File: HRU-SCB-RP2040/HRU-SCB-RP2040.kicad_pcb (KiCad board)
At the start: 2 copper layers, 42 x 55 mm, 60 parts, among them J1 Conn_01x03_Pin, J10 Conn_01x03_Pin, J11 Conn_01x03_Pin, J12 Conn_01x03_Pin, J13 Conn_01x03_Pin, J14 Conn_01x03_Pin, J15 Conn_01x03_Pin, J16 Conn_01x03_Pin, J17 Conn_01x03_Pin, J18 Conn_01x03_Pin, J19 Conn_01x03_Pin, J2 Conn_01x03_Pin, J20 Conn_01x03_Pin, J21 Conn_01x03_Pin, J22 Conn_01x03_Pin, J23 Conn_01x03_Pin, J24 Conn_01x03_Pin, J25 Conn_01x04_Pin, J26 Conn_01x04_Pin, J27 Conn_01x04_MountingPin, J28 Conn_01x04_MountingPin, J29 Conn_02x03_Top_Bottom, J3 Conn_01x03_Pin, J30 Micro_SD_Card_Det_Hirose_DM3AT, J31 Conn_01x02_Pin, J4 Conn_01x03_Pin, J5 Conn_01x03_Pin, J6 Conn_01x03_Pin, J7 Conn_01x03_Pin, J8 Conn_01x03_Pin, J9 Conn_01x03_Pin, Q1 BSS138, Q2 BSS138, Q3 BSS138, Q4 BSS138, U1 RaspberryPi_Pico_W, U2 PCA9685PW, U3 PCA9685PW, U4 NJM7805SDL1, U5 SN65HVD11HD, U6 SN65HVD11HD

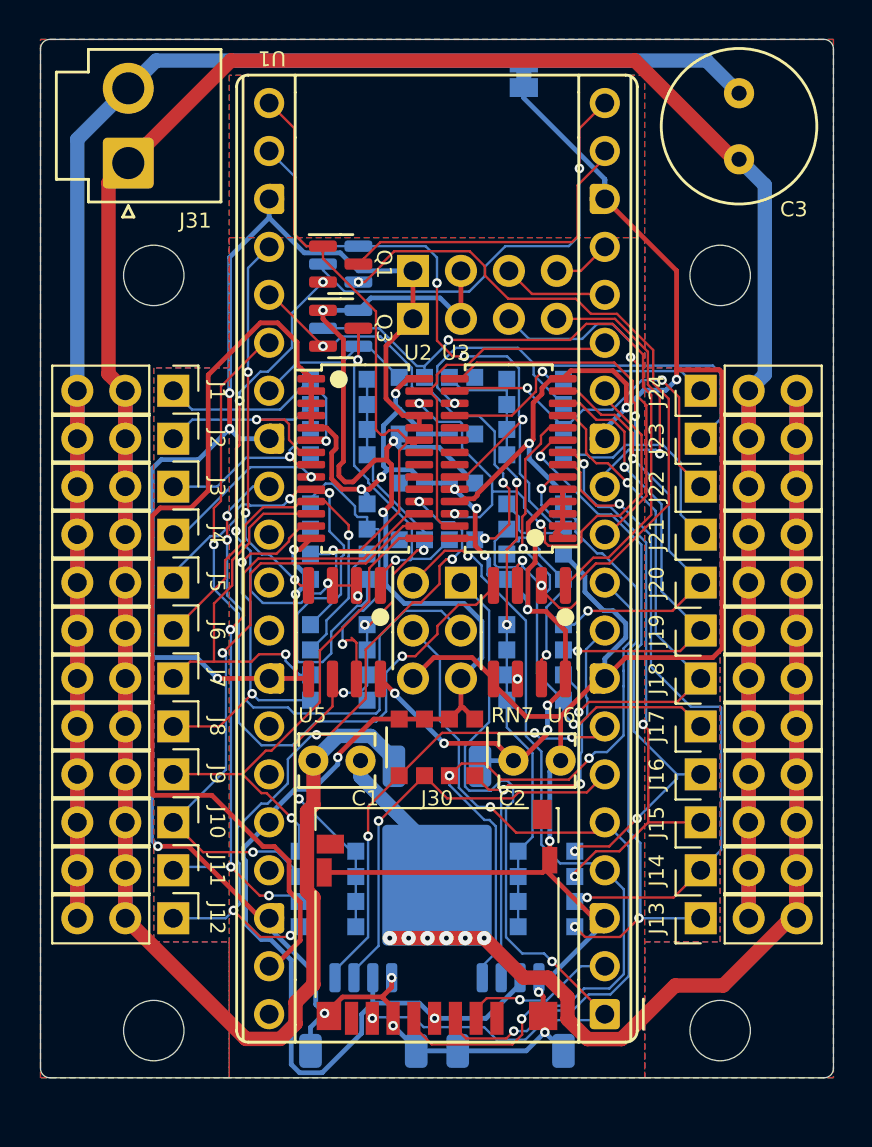
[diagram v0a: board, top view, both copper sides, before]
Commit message: Delete PWM circuit
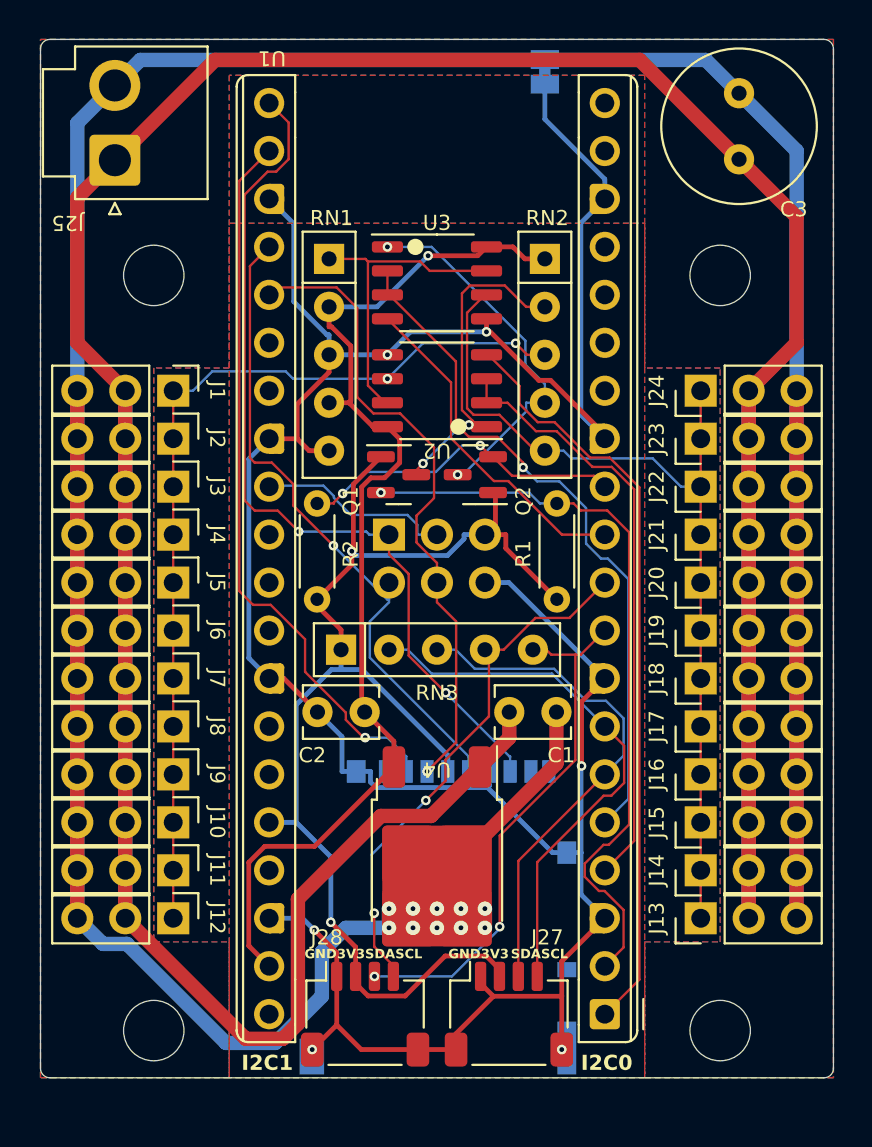
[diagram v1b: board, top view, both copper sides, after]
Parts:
- removed J30: Micro_SD_Card_Det_Hirose_DM3AT, Connector_Card:microSD_HC_Hirose_DM3D-SF
- removed J31: Conn_01x02_Pin, Connector_JST:JST_VH_B2P-VH_1x02_P3.96mm_Vertical
- removed Q3, Q4: BSS138, Package_TO_SOT_SMD:SOT-23
- removed RN10, RN11, RN7, RN8, RN9: 2.2k, Resistor_SMD:R_Array_Convex_4x1206
- removed RN4, RN5, RN6: 100, Resistor_SMD:R_Array_Convex_4x1206
- removed U5, U6: SN65HVD11HD, Package_SO:SOIC-8_3.9x4.9mm_P1.27mm
- added R1: 2.2k, Resistor_THT:R_Axial_DIN0204_L3.6mm_D1.6mm_P5.08mm_Horizontal, F.Cu at (156.3, 124.7)
- added R2: 2.2k, Resistor_THT:R_Axial_DIN0204_L3.6mm_D1.6mm_P5.08mm_Horizontal, F.Cu at (143.7, 124.7)
- J25: value Conn_01x04_Pin -> Conn_01x02_Pin; footprint Connector_PinHeader_2.54mm:PinHeader_1x04_P2.54mm_Vertical -> Connector_JST:JST_VH_B2P-VH_1x02_P3.96mm_Vertical; moved to F.Cu
- J26: value Conn_01x04_Pin -> Micro_SD_Card_Det_Hirose_DM3AT; footprint Connector_PinHeader_2.54mm:PinHeader_1x04_P2.54mm_Vertical -> Connector_Card:microSD_HC_Hirose_DM3AT-SF-PEJM5
- J27, J28, Q2, U4: moved to F.Cu
- RN1, RN2, RN3: value 100 -> 2.2k; footprint Resistor_SMD:R_Array_Convex_4x1206 -> Resistor_THT:R_Array_SIP5; moved to F.Cu
- U2, U3: value PCA9685PW -> MAX485E; footprint Package_SO:TSSOP-28_4.4x9.7mm_P0.65mm -> Package_SO:SOP-8_3.9x4.9mm_P1.27mm
- moved J26 31.7 mm to (150.1, 141.5), turned to 180 degrees
- moved RN2 24.0 mm to (155.7, 106.6), turned to -90 degrees
- moved J25 16.8 mm to (132.9, 101.4), turned to 90 degrees
- moved Q2 13.2 mm to (152.0, 118.1)
- moved RN3 12.7 mm to (144.9, 127.3)
- moved Q1 11.6 mm to (148.0, 118.1)
- moved C1 10.7 mm to (153.8, 130.6)
- moved U3 10.1 mm to (150.0, 107.9), turned to 0 degrees
- moved RN1 8.39 mm to (144.3, 106.6), turned to -90 degrees
- moved C2 8.29 mm to (146.2, 130.6), turned to 180 degrees
- moved J27 7.71 mm to (153.8, 146.6), turned to 0 degrees
- moved J28 7.71 mm to (146.2, 146.6), turned to 0 degrees
- moved U2 5.23 mm to (150.0, 113.6), turned to 180 degrees
- moved J29 4.58 mm to (147.5, 121.2), turned to -90 degrees
- moved JP1 1.13 mm to (155.7, 96.7)
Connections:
- J1 pad 1: /ServoPort/SIG.1 -> /ServoPort/SERVO.SERIAL0
- J10 pad 1: /ServoPort/SIG.10 -> /ServoPort/SERVO.SERIAL0
- J11 pad 1: /ServoPort/SIG.11 -> /ServoPort/SERVO.SERIAL0
- J12 pad 1: /ServoPort/SIG.12 -> /ServoPort/SERVO.SERIAL0
- J13 pad 1: /ServoPort/SIG.13 -> /ServoPort/SERVO.SERIAL1
- J14 pad 1: /ServoPort/SIG.14 -> /ServoPort/SERVO.SERIAL1
- J15 pad 1: /ServoPort/SIG.15 -> /ServoPort/SERVO.SERIAL1
- J16 pad 1: /ServoPort/SIG.16 -> /ServoPort/SERVO.SERIAL1
- J17 pad 1: /ServoPort/SIG.17 -> /ServoPort/SERVO.SERIAL1
- J18 pad 1: /ServoPort/SIG.18 -> /ServoPort/SERVO.SERIAL1
- J19 pad 1: /ServoPort/SIG.19 -> /ServoPort/SERVO.SERIAL1
- J2 pad 1: /ServoPort/SIG.2 -> /ServoPort/SERVO.SERIAL0
- J20 pad 1: /ServoPort/SIG.20 -> /ServoPort/SERVO.SERIAL1
- J21 pad 1: /ServoPort/SIG.21 -> /ServoPort/SERVO.SERIAL1
- J22 pad 1: /ServoPort/SIG.22 -> /ServoPort/SERVO.SERIAL1
- J23 pad 1: /ServoPort/SIG.23 -> /ServoPort/SERVO.SERIAL1
- J24 pad 1: /ServoPort/SIG.24 -> /ServoPort/SERVO.SERIAL1
- J25 pad 1: GND -> VCC
- J25 pad 2: +3V3 -> GNDPWR
- J26 pad 1: GND -> unconnected-(J26-DAT2-Pad1)
- J26 pad 2: +3V3 -> /SPI.CS.SD
- J26 pad 3: /UART1.TX -> /SPI.MOSI
- J26 pad 4: /UART1.RX -> +3V3
- J3 pad 1: /ServoPort/SIG.3 -> /ServoPort/SERVO.SERIAL0
- J4 pad 1: /ServoPort/SIG.4 -> /ServoPort/SERVO.SERIAL0
- J5 pad 1: /ServoPort/SIG.5 -> /ServoPort/SERVO.SERIAL0
- J6 pad 1: /ServoPort/SIG.6 -> /ServoPort/SERVO.SERIAL0
- J7 pad 1: /ServoPort/SIG.7 -> /ServoPort/SERVO.SERIAL0
- J8 pad 1: /ServoPort/SIG.8 -> /ServoPort/SERVO.SERIAL0
- J9 pad 1: /ServoPort/SIG.9 -> /ServoPort/SERVO.SERIAL0
- Q1 pad 1: /SERVO.SERIAL0.EN -> +3V3
- Q1 pad 2: Net-(Q1-S) -> /SERVO.SERIAL0.RX
- Q1 pad 3: /SERVO.SERIAL0.DE -> Net-(Q1-D)
- Q2 pad 1: /SERVO.SERIAL1.EN -> +3V3
- Q2 pad 2: Net-(Q2-S) -> /SERVO.SERIAL1.RX
- Q2 pad 3: /SERVO.SERIAL1.DE -> Net-(Q2-D)
- RN1 pad 1: /ServoPort/SIG.4 -> /ServoPort/SERVO.NULL
- RN1 pad 2: /ServoPort/SIG.3 -> +5V
- RN1 pad 3: /ServoPort/SIG.2 -> GND
- RN1 pad 4: /ServoPort/SIG.1 -> +5V
- RN1 pad 5: /ServoPort/SERVO.SERIAL0 -> GND
- RN2 pad 1: /ServoPort/SIG.8 -> +5V
- RN2 pad 2: /ServoPort/SIG.7 -> Net-(Q1-D)
- RN2 pad 3: /ServoPort/SIG.6 -> /ServoPort/SERVO.SERIAL0
- RN2 pad 4: /ServoPort/SIG.5 -> Net-(Q2-D)
- RN2 pad 5: /ServoPort/SERVO.SERIAL0 -> /ServoPort/SERVO.SERIAL1
- RN3 pad 1: /ServoPort/SIG.12 -> +3V3
- RN3 pad 2: /ServoPort/SIG.11 -> /I2C0.SCL
- RN3 pad 3: /ServoPort/SIG.10 -> /I2C0.SDA
- RN3 pad 4: /ServoPort/SIG.9 -> /I2C1.SCL
- RN3 pad 5: /ServoPort/SERVO.SERIAL0 -> /I2C1.SDA
- U1 pad 1: /SPI.MISO -> /SERVO.SERIAL0.TX
- U1 pad 11: /UART1.TX -> /SERVO.SERIAL1.TX
- U1 pad 12: /UART1.RX -> /SERVO.SERIAL1.RX
- U1 pad 14: /PIO.0 -> unconnected-(U1-GPIO10-Pad14)
- U1 pad 15: /PIO.1 -> unconnected-(U1-GPIO11-Pad15)
- U1 pad 16: /UART0.TX -> unconnected-(U1-GPIO12-Pad16)
- U1 pad 17: /UART0.RX -> unconnected-(U1-GPIO13-Pad17)
- U1 pad 19: /SERVO.SERIAL0.DE -> unconnected-(U1-GPIO14-Pad19)
- U1 pad 2: /SPI.CS.SD -> /SERVO.SERIAL0.RX
- U1 pad 20: /SERVO.SERIAL1.DE -> unconnected-(U1-GPIO15-Pad20)
- U1 pad 21: /SERVO.SERIAL0.EN -> /SPI.MISO
- U1 pad 22: /SERVO.SERIAL1.EN -> /SPI.CS.SD
- U1 pad 24: /PIO.2 -> /SPI.CLK
- U1 pad 25: /PIO.3 -> /SPI.MOSI
- U1 pad 26: /PIO.4 -> unconnected-(U1-GPIO20-Pad26)
- U1 pad 27: /PIO.5 -> unconnected-(U1-GPIO21-Pad27)
- U1 pad 4: /SPI.CLK -> /SERVO.SERIAL0.DE
- U1 pad 5: /SPI.MOSI -> /SERVO.SERIAL1.DE
- U2 pad 1: +5V -> Net-(Q1-D)
- U2 pad 2: +5V -> /SERVO.SERIAL0.DE
- U2 pad 3: +5V -> /SERVO.SERIAL0.DE
- U2 pad 4: +5V -> /SERVO.SERIAL0.TX
- U2 pad 5: +5V -> GND
- U2 pad 6: /ServoPort/SIG.1 -> /ServoPort/SERVO.SERIAL0
- U2 pad 7: /ServoPort/SIG.2 -> /ServoPort/SERVO.NULL
- U2 pad 8: /ServoPort/SIG.3 -> +5V
- U3 pad 1: +5V -> Net-(Q2-D)
- U3 pad 2: +5V -> /SERVO.SERIAL1.DE
- U3 pad 3: +5V -> /SERVO.SERIAL1.DE
- U3 pad 4: +5V -> /SERVO.SERIAL1.TX
- U3 pad 5: +5V -> GND
- U3 pad 6: /ServoPort/SIG.13 -> /ServoPort/SERVO.SERIAL1
- U3 pad 7: /ServoPort/SIG.14 -> /ServoPort/SERVO.NULL
- U3 pad 8: /ServoPort/SIG.15 -> +5V
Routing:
- net GND: track 233.0 -> 150.1 mm, vias 15 -> 6
- net +5V: track 118.0 -> 58.3 mm, vias 11 -> 1
- net /SERVO.SERIAL0.EN: track 48.3 -> 0.00 mm, vias 1 -> 0
- net Net-(Q2-S): track 45.1 -> 0.00 mm, vias 3 -> 0
- net /SERVO.SERIAL1.EN: track 41.4 -> 0.00 mm, vias 3 -> 0
- net /PIO.4: track 41.0 -> 0.00 mm, vias 2 -> 0
- net /SERVO.SERIAL0.TX: track 0.00 -> 40.2 mm
- net /SERVO.SERIAL0.RX: track 0.00 -> 39.6 mm, vias 0 -> 1
- net /ServoPort/SIG.12: track 37.0 -> 0.00 mm, vias 5 -> 0
- net /ServoPort/SIG.14: track 34.8 -> 0.00 mm, vias 2 -> 0
- net Net-(Q4-D): track 34.8 -> 0.00 mm, vias 1 -> 0
- net /ServoPort/SIG.13: track 34.7 -> 0.00 mm, vias 3 -> 0
- net /ServoPort/SIG.11: track 34.0 -> 0.00 mm, vias 3 -> 0
- net /ServoPort/SIG.10: track 33.0 -> 0.00 mm, vias 2 -> 0
- net GNDPWR: track 203.3 -> 235.0 mm, vias 6 -> 10
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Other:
- board text removed: "RX"
- board text removed: "TX"
- board text removed: "UART0"
- board text removed: "UART1"

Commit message: Update design for hand soldering friendly
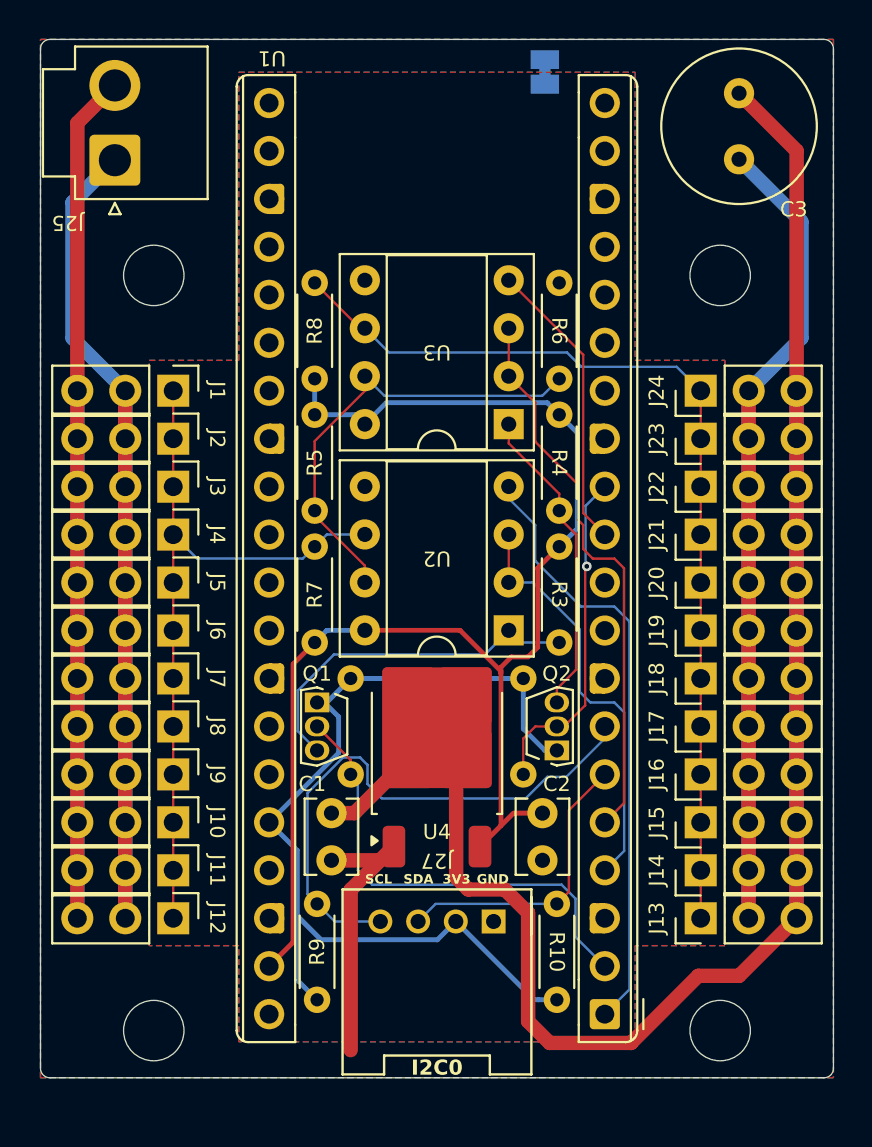
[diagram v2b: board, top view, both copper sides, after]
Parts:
- removed J26: Micro_SD_Card_Det_Hirose_DM3AT, Connector_Card:microSD_HC_Hirose_DM3AT-SF-PEJM5
- removed J28: Conn_01x04_MountingPin, Connector_JST:JST_SH_SM04B-SRSS-TB_1x04-1MP_P1.00mm_Horizontal
- removed J29: Conn_02x03_Top_Bottom, Connector_PinHeader_2.54mm:PinHeader_2x03_P2.54mm_Vertical
- removed RN1, RN2, RN3: 2.2k, Resistor_THT:R_Array_SIP5
- added R10: 2.2k, Resistor_THT:R_Axial_DIN0204_L3.6mm_D1.6mm_P5.08mm_Horizontal, F.Cu at (156.3, 140.8)
- added R3: 2.2k, Resistor_THT:R_Axial_DIN0204_L3.6mm_D1.6mm_P5.08mm_Horizontal, F.Cu at (156.5, 121.9)
- added R4: 2.2k, Resistor_THT:R_Axial_DIN0204_L3.6mm_D1.6mm_P5.08mm_Horizontal, F.Cu at (156.5, 114.9)
- added R5: 2.2k, Resistor_THT:R_Axial_DIN0204_L3.6mm_D1.6mm_P5.08mm_Horizontal, F.Cu at (143.5, 114.9)
- added R6: 2.2k, Resistor_THT:R_Axial_DIN0204_L3.6mm_D1.6mm_P5.08mm_Horizontal, F.Cu at (156.5, 113.0)
- added R7: 2.2k, Resistor_THT:R_Axial_DIN0204_L3.6mm_D1.6mm_P5.08mm_Horizontal, F.Cu at (143.5, 126.9)
- added R8: 2.2k, Resistor_THT:R_Axial_DIN0204_L3.6mm_D1.6mm_P5.08mm_Horizontal, F.Cu at (143.5, 113.0)
- added R9: 2.2k, Resistor_THT:R_Axial_DIN0204_L3.6mm_D1.6mm_P5.08mm_Horizontal, F.Cu at (143.7, 140.8)
- J27: value Conn_01x04_MountingPin -> Conn_01x04_Pin; footprint Connector_JST:JST_SH_SM04B-SRSS-TB_1x04-1MP_P1.00mm_Horizontal -> OPL_Connector:HW4-2.0-90D
- Q1, Q2: value BSS138 -> NchFET; footprint Package_TO_SOT_SMD:SOT-23 -> Package_TO_SOT_THT:TO-92S
- R1, R2: moved to B.Cu
- U2, U3: footprint Package_SO:SOP-8_3.9x4.9mm_P1.27mm -> Package_DIP:DIP-8_W7.62mm_Socket
- moved Q2 15.2 mm to (156.3, 132.7), turned to 90 degrees
- moved U2 13.2 mm to (153.8, 126.3)
- moved Q1 12.8 mm to (143.7, 130.1), turned to -90 degrees
- moved C1 12.3 mm to (144.4, 138.5), turned to 90 degrees
- moved R1 11.7 mm to (145.4, 128.8), turned to -90 degrees
- moved R2 11.7 mm to (154.6, 128.8), turned to -90 degrees
- moved C2 10.8 mm to (155.6, 136.0), turned to -90 degrees
- moved U3 8.39 mm to (153.8, 115.4), turned to 180 degrees
- moved U4 5.87 mm to (150.0, 132.7), turned to 90 degrees
- moved J27 4.18 mm to (150.0, 144.9), turned to 180 degrees
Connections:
- U1 pad 10: /I2C1.SCL -> unconnected-(U1-GPIO7-Pad10)
- U1 pad 21: /SPI.MISO -> unconnected-(U1-GPIO16-Pad21)
- U1 pad 22: /SPI.CS.SD -> unconnected-(U1-GPIO17-Pad22)
- U1 pad 24: /SPI.CLK -> unconnected-(U1-GPIO18-Pad24)
- U1 pad 25: /SPI.MOSI -> unconnected-(U1-GPIO19-Pad25)
- U1 pad 29: /SPI.CSn -> unconnected-(U1-GPIO22-Pad29)
- U1 pad 9: /I2C1.SDA -> unconnected-(U1-GPIO6-Pad9)
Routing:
- net GND: track 150.1 -> 0.00 mm, vias 6 -> 0
- net VCC: track 213.1 -> 156.2 mm
- net /SPI.MISO: track 46.3 -> 0.00 mm, vias 2 -> 0
- net GNDPWR: track 235.0 -> 192.3 mm, vias 10 -> 0
- net /SPI.CS.SD: track 38.5 -> 0.00 mm, vias 1 -> 0
- net /SPI.CLK: track 35.3 -> 0.00 mm, vias 1 -> 0
- net /SPI.MOSI: track 34.2 -> 0.00 mm, vias 1 -> 0
- net /I2C1.SDA: track 28.3 -> 0.00 mm, vias 2 -> 0
- net /I2C1.SCL: track 28.2 -> 0.00 mm, vias 2 -> 0
- net +3V3: track 67.4 -> 51.8 mm, vias 2 -> 0
- net +5V: track 58.3 -> 73.5 mm, vias 1 -> 0
- net /SERVO.SERIAL0.RX: track 39.6 -> 24.9 mm, vias 1 -> 0
- net /I2C0.SDA: track 27.4 -> 15.6 mm
- net /SPI.CSn: track 10.3 -> 0.00 mm
- net /ServoPort/SERVO.SERIAL0: track 49.3 -> 39.1 mm, vias 2 -> 0
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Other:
- board text removed: "CLK"
- board text removed: "CS"
- board text removed: "I2C1"
- board text removed: "MISO"
- board text removed: "MOSI"

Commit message: Update DCDC for DIP soldering
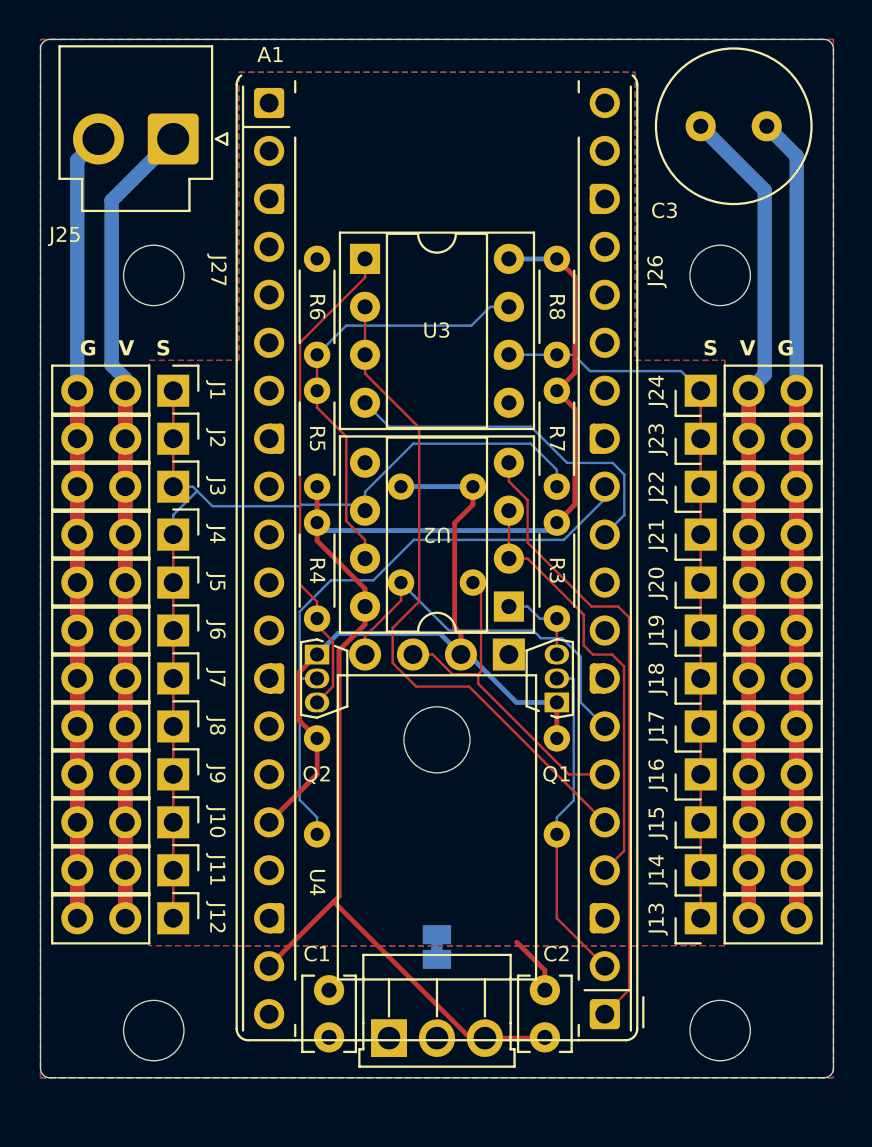
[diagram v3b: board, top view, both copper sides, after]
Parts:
- removed U1: RaspberryPi_Pico_W, Module_RaspberryPi_Pico:RaspberryPi_Pico_Common_THT
- added A1: RaspberryPi_Pico_W, Module_RaspberryPi_Pico:RaspberryPi_Pico_W_Virtual, F.Cu at (150.0, 122.4)
- added J26: Pico_Socket_A, Module_RaspberryPi_Pico:RaspberryPi_Pico_PinSocket_1x20_P2.54mm_Vertical, F.Cu at (158.9, 146.6)
- added J28: Conn_01x04_Pin, mymod:PinHeader_1x04_P2.54mm_Vertical_SmallCourtyard, B.Cu at (153.8, 127.6)
- J27: value Conn_01x04_Pin -> Pico_Socket_B; footprint OPL_Connector:HW4-2.0-90D -> Module_RaspberryPi_Pico:RaspberryPi_Pico_PinSocket_1x20_P2.54mm_Vertical
- R1, R2, R4, R5, R6: value 2.2k -> 5.1k
- R10, R9: moved to B.Cu
- U4: value NJM7805SDL1 -> NJM7805FA; footprint Package_TO_SOT_SMD:TO-252-2 -> Package_TO_SOT_THT:TO-220F-3_Horizontal_TabDown
- moved J27 47.4 mm to (141.1, 98.4), turned to 0 degrees
- moved JP1 46.7 mm to (150.0, 143.1), turned to 90 degrees
- moved R7 18.5 mm to (156.3, 113.6), turned to -90 degrees
- moved R10 17.6 mm to (151.9, 123.8), turned to 90 degrees
- moved R9 17.6 mm to (148.1, 123.8), turned to 90 degrees
- moved U4 15.4 mm to (147.5, 147.9), turned to 0 degrees
- moved R8 14.3 mm to (156.3, 106.6), turned to -90 degrees
- moved R4 14.0 mm to (143.7, 120.6)
- moved Q2 13.7 mm to (143.7, 127.6), turned to -90 degrees
- moved R6 12.9 mm to (143.7, 111.7)
- moved Q1 12.7 mm to (156.3, 130.1), turned to 90 degrees
- moved C2 11.9 mm to (155.7, 147.9), turned to 90 degrees
- moved U3 11.6 mm to (146.2, 106.6), turned to 0 degrees
- moved R1 11.4 mm to (156.3, 132.0)
- moved R2 11.4 mm to (143.7, 132.0)
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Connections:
- J27 pad 1: GND -> unconnected-(J27-GPIO16-Pad1)
- J27 pad 2: +3V3 -> unconnected-(J27-GPIO17-Pad2)
- J27 pad 3: /I2C0.SDA -> GND
- J27 pad 4: /I2C0.SCL -> unconnected-(J27-GPIO18-Pad4)
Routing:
- net GNDPWR: track 192.3 -> 140.2 mm
- net /SERVO.SERIAL1.RX: track 18.0 -> 32.4 mm, vias 1 -> 0
- net Net-(Q1-D): track 19.0 -> 4.71 mm
- net VCC: track 156.2 -> 142.5 mm
- net /ServoPort/SERVO.SERIAL0: track 39.1 -> 52.5 mm
- net /ServoPort/SERVO.SERIAL1: track 50.8 -> 38.9 mm
- net +3V3: track 51.8 -> 40.5 mm
- net /I2C0.SCL: track 29.8 -> 20.0 mm
- net Net-(Q2-D): track 16.6 -> 26.0 mm
- net /SERVO.SERIAL0.RX: track 24.9 -> 17.5 mm
- net /SERVO.SERIAL1.DE: track 29.8 -> 35.4 mm
- net GND: track 0.00 -> 4.21 mm
- net /SERVO.SERIAL1.TX: track 15.6 -> 18.9 mm
- net /I2C0.SDA: track 15.6 -> 18.2 mm
- net /ServoPort/SERVO.NULL: track 24.2 -> 23.1 mm
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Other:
- board text added: "G V S"
- board text added: "HRU-SCB-RP2040 github.com/rmf-hru-wg/HRUServoController"
- board text added: "S V G"
- board text removed: "HRU-SCB-RP2040 github.com/rmf-hru-wg"
- board text removed: "I2C0"
